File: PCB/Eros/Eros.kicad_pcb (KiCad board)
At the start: 2 copper layers, 107 parts, among them J1 USB_C_PowerOnly_6P, J2 UART, J3 Li-ion, J4 Conn_01x08_Socket, J5 Conn_01x03_Socket, J6 Micro_SD_Card, J7 AudioJack3, Q1 BC817, SW1 SW_Push, SW2 SW_Push, SW3 SW_Push, SW4 SW_Push, SW5 SW_Push, SW6 SW_SPDT, U1 ESP32-WROOM-32E, U2 LIS3DH, U3 MCP73831-2-OT, U4 AP2112K-3.3, U5 ADS1115IDGS, U6 MCP100-315D, U7 AD8232, U8 OPA333xxD

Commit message: Wstępne ułożenie komponentów
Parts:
- R13, R14: value 100k -> 1M
- moved U2 162.8 mm to (192.0, 102.5), turned to -135 degrees
- moved SW2 156.4 mm to (195.1, 68.0), turned to 90 degrees
- moved TP5 156.2 mm to (181.5, 100.0)
- moved R31 152.4 mm to (185.5, 98.0), turned to 90 degrees
- moved TP2 143.9 mm to (158.0, 116.5)
- moved U4 142.2 mm to (193.5, 119.0), turned to 90 degrees
- moved R34 138.7 mm to (171.8, 93.0)
- moved SW1 134.8 mm to (174.0, 100.5)
- moved TP4 133.1 mm to (151.0, 114.0)
- moved TP1 131.8 mm to (148.5, 103.0)
- moved R26 129.7 mm to (163.0, 74.5), turned to 90 degrees
- moved U6 129.2 mm to (193.5, 125.0), turned to -90 degrees
- moved C15 128.3 mm to (188.5, 119.5)
- moved C17 125.0 mm to (190.0, 113.5)
- moved C7 125.0 mm to (188.0, 102.5), turned to 90 degrees
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- renumbered TP11 to TP6
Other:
- board outline added: 72.2 x 80.5 mm

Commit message: Poprawa schematu oraz ulozenie komponentow
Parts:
- removed C4: 100n, Capacitor_SMD:C_0402_1005Metric_Pad0.74x0.62mm_HandSolder
- removed JP3, JP4: SolderJumper_2_Open, Jumper:SolderJumper-2_P1.3mm_Open_Pad1.0x1.5mm
- removed R29, R30: R, Resistor_SMD:R_0402_1005Metric_Pad0.72x0.64mm_HandSolder
- removed R32, R4: 10k, Resistor_SMD:R_0402_1005Metric_Pad0.72x0.64mm_HandSolder
- removed R34: 10k, Resistor_SMD:R_01005_0402Metric_Pad0.57x0.30mm_HandSolder
- removed SW3: SW_Push, Button_Switch_THT:SW_Tactile_SPST_Angled_PTS645Vx39-2LFS
- removed TP6: TestPoint, TestPoint:TestPoint_Pad_D1.5mm
- removed U5: ADS1115IDGS, Package_SO:TSSOP-10_3x3mm_P0.5mm
- removed U7: AD8232, AD8232:QFN-20_EP_4x4_Pitch0.5mm
- removed U8: OPA333xxD, Package_SO:SOIC-8_3.9x4.9mm_P1.27mm
- added C31: 100n, Capacitor_SMD:C_0402_1005Metric_Pad0.74x0.62mm_HandSolder, F.Cu at (170.5, 83.0)
- added C32: 1n, Capacitor_SMD:C_0402_1005Metric_Pad0.74x0.62mm_HandSolder, F.Cu at (172.5, 78.5)
- added C33: 1n, Capacitor_SMD:C_0402_1005Metric_Pad0.74x0.62mm_HandSolder, F.Cu at (172.5, 81.0)
- added C34: 1.5n, Capacitor_SMD:C_0402_1005Metric_Pad0.74x0.62mm_HandSolder, F.Cu at (183.4, 80.8)
- added C35: 100n, Capacitor_SMD:C_0402_1005Metric_Pad0.74x0.62mm_HandSolder, F.Cu at (178.0, 95.0)
- added C36: 10u, Capacitor_SMD:C_0603_1608Metric_Pad1.08x0.95mm_HandSolder, F.Cu at (174.0, 98.5)
- added C37: 47p, Capacitor_SMD:C_0402_1005Metric_Pad0.74x0.62mm_HandSolder, F.Cu at (164.5, 83.5)
- added C38: 47p, Capacitor_SMD:C_0402_1005Metric_Pad0.74x0.62mm_HandSolder, F.Cu at (161.5, 84.0)
- added C39: 100n, Capacitor_SMD:C_0402_1005Metric_Pad0.74x0.62mm_HandSolder, F.Cu at (182.5, 94.0)
- added C40: 1u, Capacitor_SMD:C_0402_1005Metric_Pad0.74x0.62mm_HandSolder, F.Cu at (181.0, 94.0)
- added C41: 100n, Capacitor_SMD:C_0402_1005Metric_Pad0.74x0.62mm_HandSolder, F.Cu at (188.5, 93.9)
- added C42: 1u, Capacitor_SMD:C_0402_1005Metric_Pad0.74x0.62mm_HandSolder, F.Cu at (187.0, 93.9)
- added D1: BAV99, Package_TO_SOT_SMD:SOT-23, F.Cu at (172.0, 87.0)
- added D4: BAV99, Package_TO_SOT_SMD:SOT-23, F.Cu at (165.0, 86.5)
- added D5: BAV99, Package_TO_SOT_SMD:SOT-23, F.Cu at (172.0, 92.5)
- added D6: BAV99, Package_TO_SOT_SMD:SOT-23, F.Cu at (164.5, 92.0)
- added FB2: FerriteBead(600om), Inductor_SMD:L_0402_1005Metric_Pad0.77x0.64mm_HandSolder, F.Cu at (185.0, 93.5)
- added IC1: ADS1292RIPBS, ADS1292:QFP50P700X700X120-32N, F.Cu at (184.0, 87.0)
- added R33: 10k, Resistor_SMD:R_0402_1005Metric_Pad0.72x0.64mm_HandSolder, F.Cu at (199.5, 103.5)
- C19: value 1n -> 47n
- C20: value 10n -> 47n
- C21: value 1.5n -> 2.2u
- C22: value 0.33u -> 2.2u
- C23: value 0.33u -> 22u
- C26, C27: value C -> 2.2n
- C29, C30: value 100n -> 2.2n
- FB1: value FerriteBead -> FerriteBead(120om)
- J3: footprint BHC-18650-1P COMF:BatteryHolder_MPD_BH-18650-PC -> Connector_JST:JST_PH_B2B-PH-K_1x02_P2.00mm_Vertical; moved to F.Cu
- J5: value Conn_01x03_Socket -> AudioJack3; footprint Connector_PinHeader_1.27mm:PinHeader_1x03_P1.27mm_Vertical -> Connector_Audio:Jack_3.5mm_Lumberg_1503_03_Horizontal
- J7: value AudioJack3 -> Conn_01x03_Socket; footprint Connector_Audio:Jack_3.5mm_Lumberg_1503_03_Horizontal -> Connector_PinHeader_2.54mm:PinHeader_1x03_P2.54mm_Vertical
- R15: value 180k -> 10k
- R16: value 180k -> 10M
- R18: value 10M -> 40.2k
- R19: value 360k -> 51k
- R20: value 100k -> 40.2k
- R21: value 1M -> 51k
- R22, R23: value 1M -> 10M
- R24: value 10M -> 1M
- R25, R27: value 10M -> 100k
- R26: value 1.4M -> 0R; footprint Resistor_SMD:R_0805_2012Metric_Pad1.20x1.40mm_HandSolder -> Resistor_SMD:R_0402_1005Metric_Pad0.72x0.64mm_HandSolder
- R28: value 10M -> 10k
- R31: footprint Resistor_SMD:R_01005_0402Metric_Pad0.57x0.30mm_HandSolder -> Resistor_SMD:R_0402_1005Metric_Pad0.72x0.64mm_HandSolder
- U1: footprint RF_Module:ESP32-WROOM-32D -> RF_Module:ESP32-WROOM-32E
- moved SW4 81.6 mm to (215.8, 78.2), turned to -90 degrees
- moved SW5 76.5 mm to (215.8, 88.7), turned to -90 degrees
- moved H7 69.1 mm to (213.0, 60.5)
- moved C5 67.9 mm to (208.5, 81.5), turned to -90 degrees
- moved R5 65.3 mm to (208.0, 79.0)
- moved C6 62.3 mm to (208.0, 88.0), turned to 180 degrees
- moved H6 59.7 mm to (213.0, 116.0)
- moved R6 59.1 mm to (208.0, 92.5), turned to 0 degrees
- moved TP4 57.0 mm to (166.0, 59.0), turned to 90 degrees
- moved J2 56.8 mm to (212.5, 65.9), turned to 0 degrees
- moved Buzzer1 50.8 mm to (158.5, 106.5), turned to -90 degrees
- moved Q1 41.4 mm to (156.5, 94.5), turned to -90 degrees
- moved TP1 40.6 mm to (161.5, 64.5), turned to 90 degrees
- moved C21 39.2 mm to (183.0, 92.0)
- moved R35 39.1 mm to (199.5, 59.6), turned to -90 degrees
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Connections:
- Buzzer1 pad P: VS -> +3.3V
- C10 pad 2: VS -> +3.3V
- C11 pad 2: VS -> +3.3V
- C16 pad 2: VS -> +3.3V
- C18 pad 1: ADC1 -> ADC
- C19 pad 2: Net-(U7-RLD) -> Net-(IC1-PGA1N)
- C20 pad 1: OPAMP+ -> Net-(IC1-PGA2P)
- C20 pad 2: REFOUT -> Net-(IC1-PGA2N)
- C21 pad 1: Net-(C21-Pad1) -> VCAP1
- C21 pad 2: OUTPUT -> GND
- C22 pad 1: Net-(U7-HPDRIVE) -> VCAP2
- C22 pad 2: Net-(U7-HPSENSE) -> GND
- C23 pad 1: SW -> VREFP
- C23 pad 2: REFOUT -> GND
- C24 pad 1: GND -> VREFP
- C24 pad 2: VS -> GND
- C25 pad 1: GND -> LA
- C25 pad 2: REFIN -> Net-(C25-Pad2)
- C26 pad 1: SW -> Net-(C25-Pad2)
- C26 pad 2: REFOUT -> Net-(C26-Pad2)
- C27 pad 1: GND -> IN1P
- C27 pad 2: REFIN -> Net-(C25-Pad2)
- C28 pad 1: VS -> +3.3V
- C29 pad 1: VS -> Net-(C29-Pad1)
- C29 pad 2: GND -> Net-(C29-Pad2)
- C3 pad 1: VS -> +3.3V
- C30 pad 1: Net-(U8-+) -> IN1N
- C30 pad 2: GND -> Net-(C29-Pad1)
- C7 pad 2: VS -> +3.3V
- C8 pad 2: VS -> +3.3V
- C9 pad 2: VS -> +3.3V
- D2 pad 1: VS -> +3.3V
- J2 pad 1: VS -> +3.3V
- J4 pad 1: VS -> +3.3V
- J4 pad 3: HSPI_MOSI -> VSPI_MOSI
- J4 pad 4: HSPI_CLK -> VSPI_SCK
- J4 pad 5: HSPI_CS -> DISP_CS
- J6 pad 4: VS -> +3.3V
- R1 pad 1: VS -> +3.3V
- R13 pad 1: ADC1 -> ADC
- R14 pad 1: ADC1 -> ADC
- R15 pad 1: LA -> +3.3V
- R15 pad 2: Net-(U7-+IN) -> HSPI_CS
- R16 pad 1: RA -> AVDD
- R16 pad 2: Net-(U7--IN) -> IN1P
- R17 pad 1: LA -> GND
- R17 pad 2: VS -> IN1P
- R18 pad 1: VS -> Net-(C26-Pad2)
- R18 pad 2: RA -> IN3P
- R19 pad 1: RL -> IN2P
- R19 pad 2: Net-(U7-RLD) -> LA
- R2 pad 1: VS -> +3.3V
- R20 pad 1: OPAMP- -> Net-(C29-Pad2)
- R20 pad 2: REFOUT -> IN3N
- R21 pad 1: OPAMP- -> IN2N
- R21 pad 2: OUTPUT -> RA
- R22 pad 1: Net-(C21-Pad1) -> GND
- R22 pad 2: OPAMP+ -> IN1N
- R23 pad 1: IAOUT -> AVDD
- R23 pad 2: Net-(C21-Pad1) -> IN1N
- R24 pad 1: Net-(U7-HPSENSE) -> RLDINV
- R24 pad 2: Net-(R24-Pad2) -> RLDOUT
- R25 pad 1: Net-(R24-Pad2) -> RLDINV
- R25 pad 2: IAOUT -> RL
- R26 pad 1: SW -> RLDINV
- R26 pad 2: Net-(R24-Pad2) -> RLDOUT
- R27 pad 1: REFIN -> RLDIN
- R27 pad 2: VS -> RLDINV
- R28 pad 1: REFIN -> GND
- R28 pad 2: GND -> HSPI_SCK
- R31 pad 1: VS -> +3.3V
- R31 pad 2: VSPI_CS -> DISP_CS
- R35 pad 1: VS -> +3.3V
- R36 pad 1: VS -> +3.3V
- R37 pad 1: VS -> +3.3V
- R38 pad 1: VS -> +3.3V
- R5 pad 1: VS -> +3.3V
- R6 pad 1: VS -> +3.3V
- R7 pad 1: VS -> +3.3V
- R8 pad 1: VS -> +3.3V
- TP4 pad 1: VS -> +3.3V
- U1 pad 10: BUTTON_1 -> START
- U1 pad 11: BUTTON_2 -> PWDN
- U1 pad 12: BUTTON_3 -> BUZZER
- U1 pad 13: HSPI_CLK -> HSPI_MISO
- U1 pad 14: LOD+ -> HSPI_SCK
- U1 pad 2: VS -> +3.3V
- U1 pad 29: VSPI_CS -> DISP_CS
- U1 pad 4: Net-(JP3-B) -> ADC
- U1 pad 5: unconnected-(U1-SENSOR_VN-Pad5) -> BUTTON_2
- U1 pad 6: LOD- -> DRDY
- U1 pad 7: BUZZER -> BUTTON_1
- U1 pad 8: SDN -> VSPI_CS
- U2 pad 1: VS -> +3.3V
- U2 pad 14: VS -> +3.3V
- U2 pad 8: VS -> +3.3V
- U4 pad 5: VS -> +3.3V
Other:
- board size 72.2 x 80.5 mm -> 65 x 71 mm

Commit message: dodanie stackup jlcpcb_4L_1.6mm_outer1oz_inner1oz_NOREQ
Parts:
- added R4: 10k, Resistor_SMD:R_0402_1005Metric_Pad0.72x0.64mm_HandSolder, F.Cu at (1.14, 0.49)
- C34: value 1.5n -> 47p
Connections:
- C18 pad 1: ADC -> GND
- C18 pad 2: GND -> ADC
- C34 pad 1: RLDOUT -> Net-(C34-Pad1)
- J4 pad 5: DISP_CS -> VSPI_CS
- J6 pad 2: VSPI_CS -> MICRO_SD_CS
- R14 pad 1: ADC -> GND
- R14 pad 2: GND -> ADC
- R24 pad 2: RLDOUT -> Net-(C34-Pad1)
- R25 pad 1: RLDINV -> Net-(C34-Pad1)
- R26 pad 1: RLDINV -> Net-(C34-Pad1)
- R27 pad 2: RLDINV -> Net-(C34-Pad1)
- R31 pad 2: DISP_CS -> VSPI_CS
- U1 pad 29: DISP_CS -> VSPI_CS
- U1 pad 8: VSPI_CS -> MICRO_SD_CS
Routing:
- added copper zone on In2.Cu, net +3.3V
- added copper zone on In1.Cu, net GND
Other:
- copper layers 2 -> 4

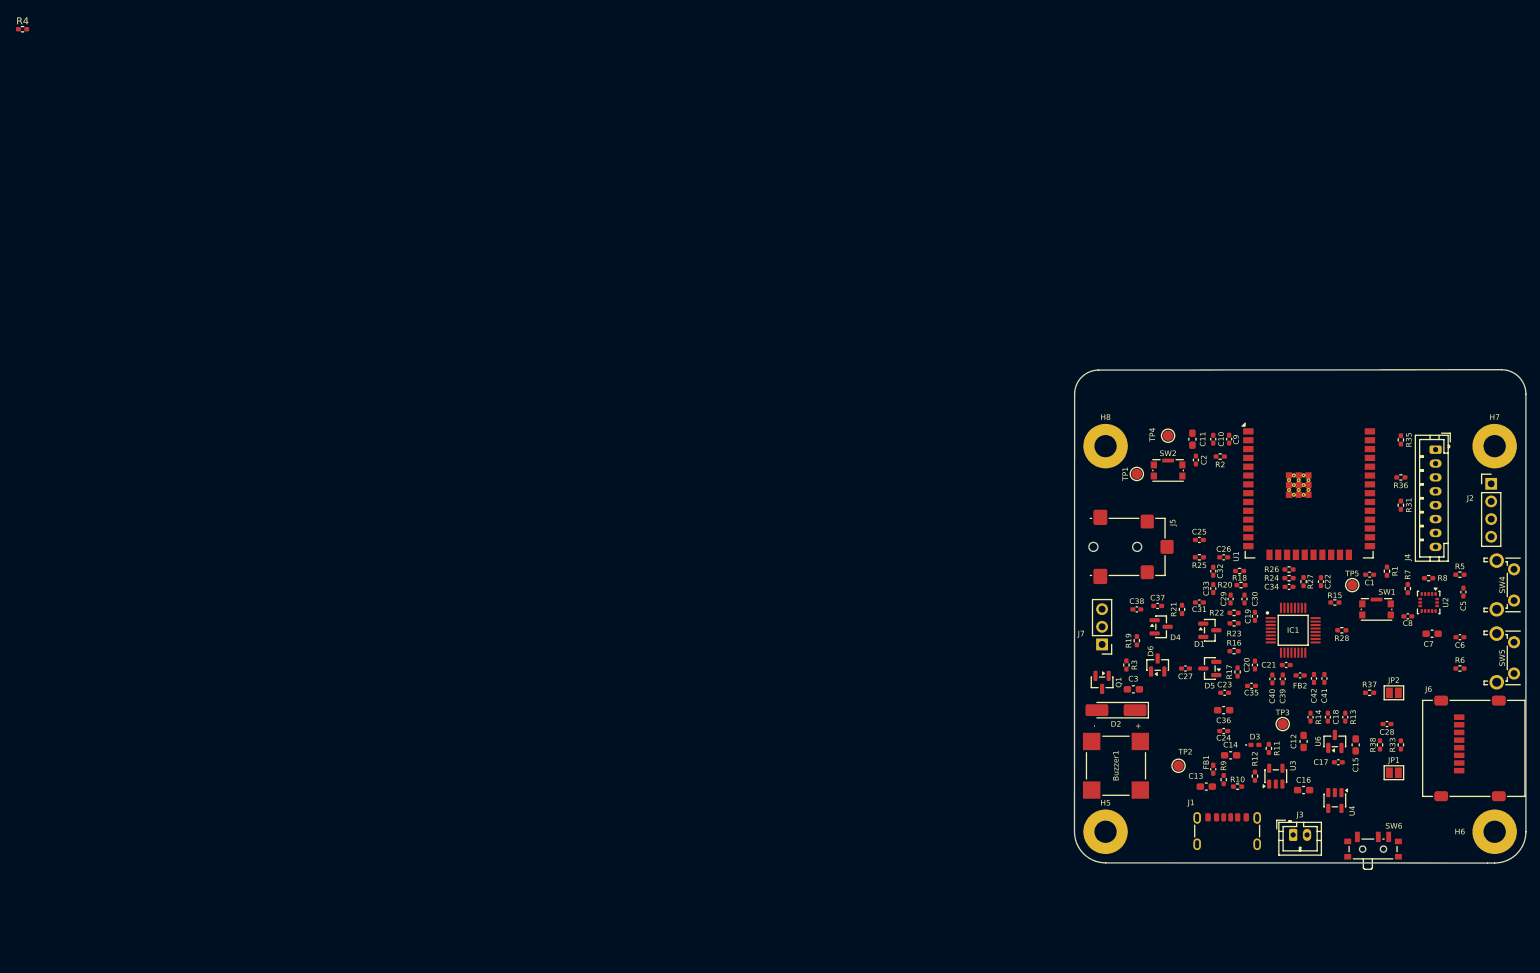
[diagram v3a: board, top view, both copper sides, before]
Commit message: podpięcie zasilania
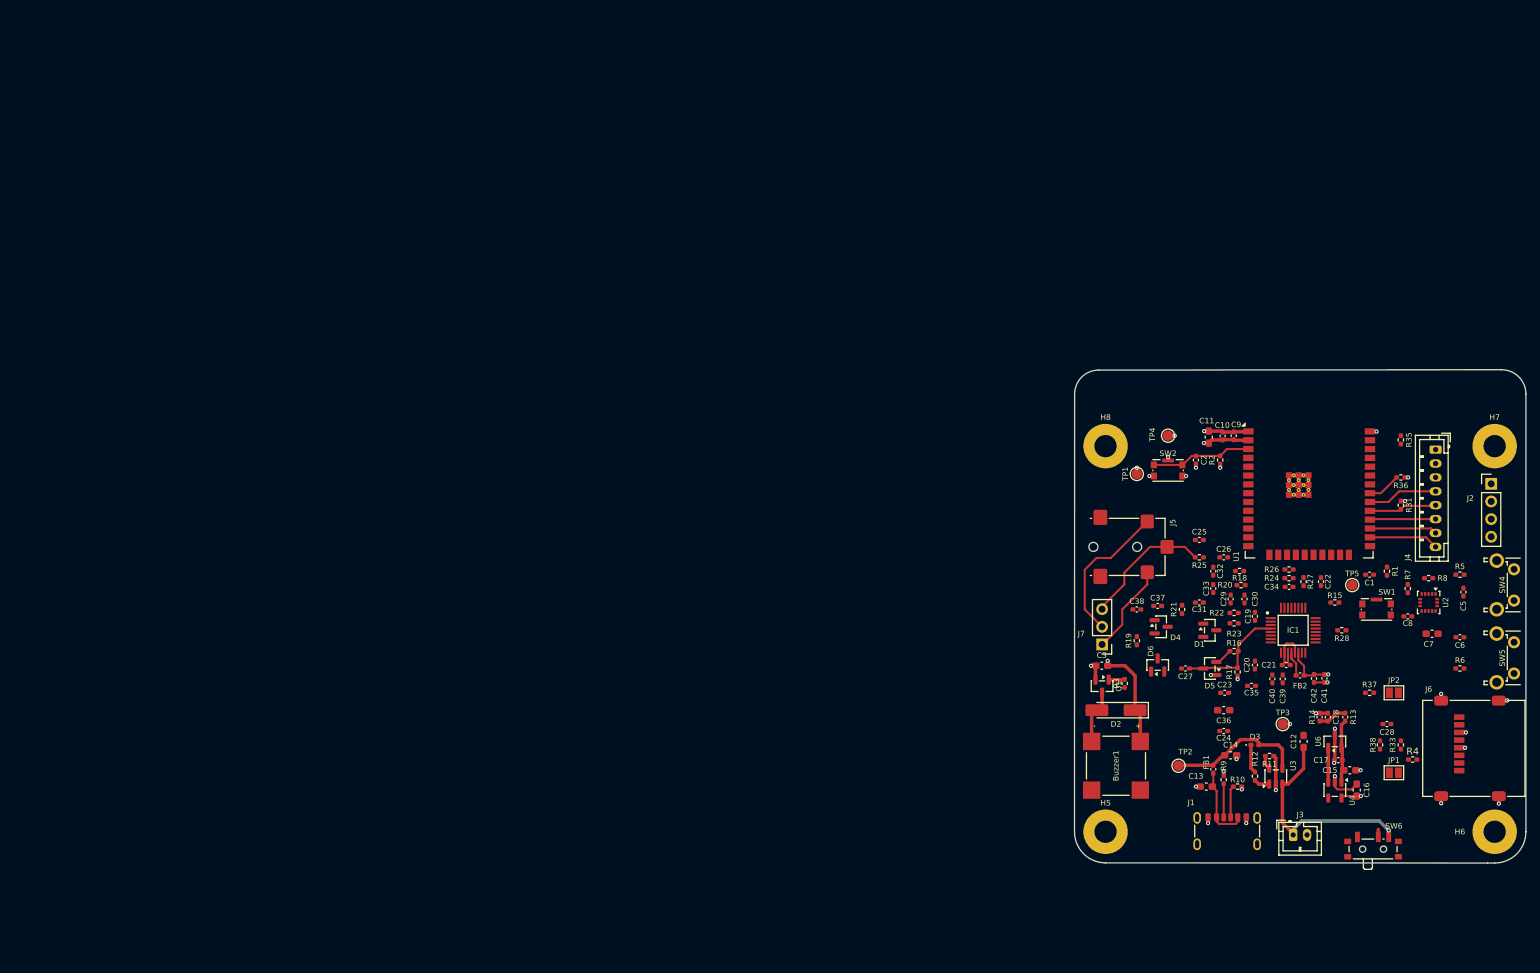
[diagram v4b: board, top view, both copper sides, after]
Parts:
- moved R4 226.0 mm to (201.2, 105.6)
- moved C16 7.65 mm to (193.2, 110.0), turned to -90 degrees
- moved C3 5.68 mm to (156.4, 92.1)
- moved C15 3.75 mm to (192.2, 107.2), turned to 180 degrees
- moved R3 2.66 mm to (159.8, 94.7), turned to 90 degrees
- moved C11 2.37 mm to (171.8, 59.2)
- moved U4 1.50 mm to (190.0, 110.0)
- moved C10 1.42 mm to (173.8, 59.0)
- moved R14 1.30 mm to (187.8, 99.5)
- moved R11 1.10 mm to (180.6, 105.1), turned to 180 degrees
- moved C9 0.82 mm to (175.4, 59.0)
- moved Q1 0.55 mm to (156.5, 95.0)
- moved R2 0.50 mm to (173.5, 62.5), turned to 90 degrees
- moved C17 0.30 mm to (190.5, 105.7)
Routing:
- net GND: track 0.00 -> 48.8 mm, vias 0 -> 28
- net +3.3V: track 0.00 -> 35.1 mm, vias 0 -> 9
- net Acc: track 0.00 -> 32.6 mm, vias 0 -> 2
- net LA: track 0.00 -> 21.1 mm
- net VBUS_FILT: track 0.00 -> 20.0 mm
- net RL: track 0.00 -> 18.9 mm
- net IN1P: track 0.00 -> 15.9 mm
- net RESET: track 0.00 -> 14.5 mm
- net RA: track 0.00 -> 13.1 mm
- net Net-(C13-Pad1): track 0.00 -> 11.4 mm
- net Net-(SW6-B): track 0.00 -> 10.4 mm
- net VSPI_SCK: track 0.00 -> 10.1 mm
- net DISP_BUSY: track 0.00 -> 10.0 mm
- net VSPI_CS: track 0.00 -> 9.79 mm
- net DISP_RST: track 0.00 -> 9.72 mm
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
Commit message: wszystko poza ads
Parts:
- removed R33: 10k, Resistor_SMD:R_0402_1005Metric_Pad0.72x0.64mm_HandSolder
- added G1: LOGO, LOGO, B.Cu at (166.2, 51.3)
- moved C29 49.9 mm to (127.6, 98.0)
- moved C30 49.9 mm to (129.6, 98.0)
- moved C33 49.9 mm to (125.1, 96.5)
- moved D1 49.9 mm to (124.6, 102.5)
- moved R20 49.9 mm to (129.1, 96.0)
- moved R22 49.9 mm to (128.1, 100.0)
- moved R23 49.9 mm to (128.1, 101.5)
- moved R4 46.8 mm to (174.4, 67.2)
- moved D5 38.6 mm to (134.1, 85.5)
- moved R16 38.6 mm to (137.6, 83.0)
- moved R17 38.6 mm to (138.1, 86.0)
- moved R19 15.6 mm to (177.1, 88.0), turned to 180 degrees
- moved C38 15.4 mm to (168.2, 70.2)
- moved TP4 12.2 mm to (155.8, 65.7), turned to 0 degrees
- moved C27 10.4 mm to (177.1, 86.6)
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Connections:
- SW2 pad SH: GND -> unconnected-(SW2-PadSH)
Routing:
- net VSPI_MOSI: track 0.00 -> 55.2 mm, vias 0 -> 1
- net BUTTON_1: track 0.00 -> 52.7 mm, vias 0 -> 2
- net BUTTON_2: track 0.00 -> 48.3 mm, vias 0 -> 2
- net VSPI_MISO: track 4.79 -> 43.5 mm, vias 0 -> 2
- net VSPI_SCK: track 10.1 -> 48.7 mm, vias 0 -> 1
- net RTC_GPIO: track 0.00 -> 38.4 mm, vias 0 -> 2
- net GND: track 48.8 -> 76.5 mm, vias 28 -> 48
- net SCL1: track 0.00 -> 25.7 mm, vias 0 -> 2
- net SDA1: track 0.00 -> 21.4 mm, vias 0 -> 2
- net RXD0: track 0.00 -> 20.6 mm, vias 0 -> 1
- net TXD0: track 0.00 -> 20.2 mm, vias 0 -> 1
- net +3.3V: track 35.1 -> 52.7 mm, vias 9 -> 23
- net HSPI_MOSI: track 0.00 -> 16.5 mm, vias 0 -> 2
- net BOOT: track 0.00 -> 14.8 mm
- net IN3P: track 0.00 -> 14.6 mm
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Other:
- board text added: "3V3"
- board text added: "EROS"
- board text added: "GND"
- board text added: "LA"
- board text added: "ON"
- board text added: "RA"
- board text added: "RL"

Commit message: ads in1p
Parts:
- moved D6 41.0 mm to (123.7, 88.7)
- moved R16 39.6 mm to (177.1, 85.9)
- moved R17 39.0 mm to (177.1, 87.0), turned to 0 degrees
- moved D4 33.7 mm to (131.3, 85.5)
- moved D1 28.1 mm to (141.9, 80.3), turned to -90 degrees
- moved D5 5.04 mm to (139.1, 85.6), turned to -90 degrees
- moved C27 2.46 mm to (175.5, 84.7)
- moved C19 1.98 mm to (179.0, 83.4)
- moved R26 1.25 mm to (183.4, 78.3)
- moved C33 1.11 mm to (124.0, 96.4)
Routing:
- net ADC: track 4.17 -> 53.9 mm, vias 0 -> 2
- net LA: track 27.0 -> 51.6 mm, vias 0 -> 2
- net Net-(C34-Pad1): track 3.01 -> 22.0 mm, vias 0 -> 2
- net HSPI_MOSI: track 16.5 -> 2.57 mm, vias 2 -> 1
- net START: track 0.00 -> 8.65 mm, vias 0 -> 1
- net RLDOUT: track 0.00 -> 6.55 mm
- net DRDY: track 0.00 -> 6.39 mm, vias 0 -> 2
- net MICRO_SD_CS: track 8.26 -> 11.8 mm, vias 1 -> 2
- net RLDINV: track 1.27 -> 4.69 mm
- net RLDIN: track 0.00 -> 3.36 mm
- net RTC_GPIO: track 38.4 -> 35.0 mm
- net Net-(IC1-PGA1N): track 0.00 -> 3.15 mm
- net BUTTON_2: track 48.3 -> 51.4 mm
- net Net-(IC1-PGA1P): track 0.00 -> 3.09 mm
- net IN1P: track 3.48 -> 6.54 mm
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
